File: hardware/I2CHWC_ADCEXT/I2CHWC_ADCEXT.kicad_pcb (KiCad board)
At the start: 2 copper layers, 66 x 99.1 mm, 23 parts, among them J1 ADC 1-8, J10 EXT, J2 ADC 9-16, J3 ADC 17-24, J4 ADC 25-32, J5 ADC 33-40, J6 ADC 41-48, J7 ADC 49-56, J8 ADC 57-64, J9 ADC, U1 4051, U2 4051, U3 4051, U4 4051, U5 4051, U6 4051, U7 4051, U8 4051

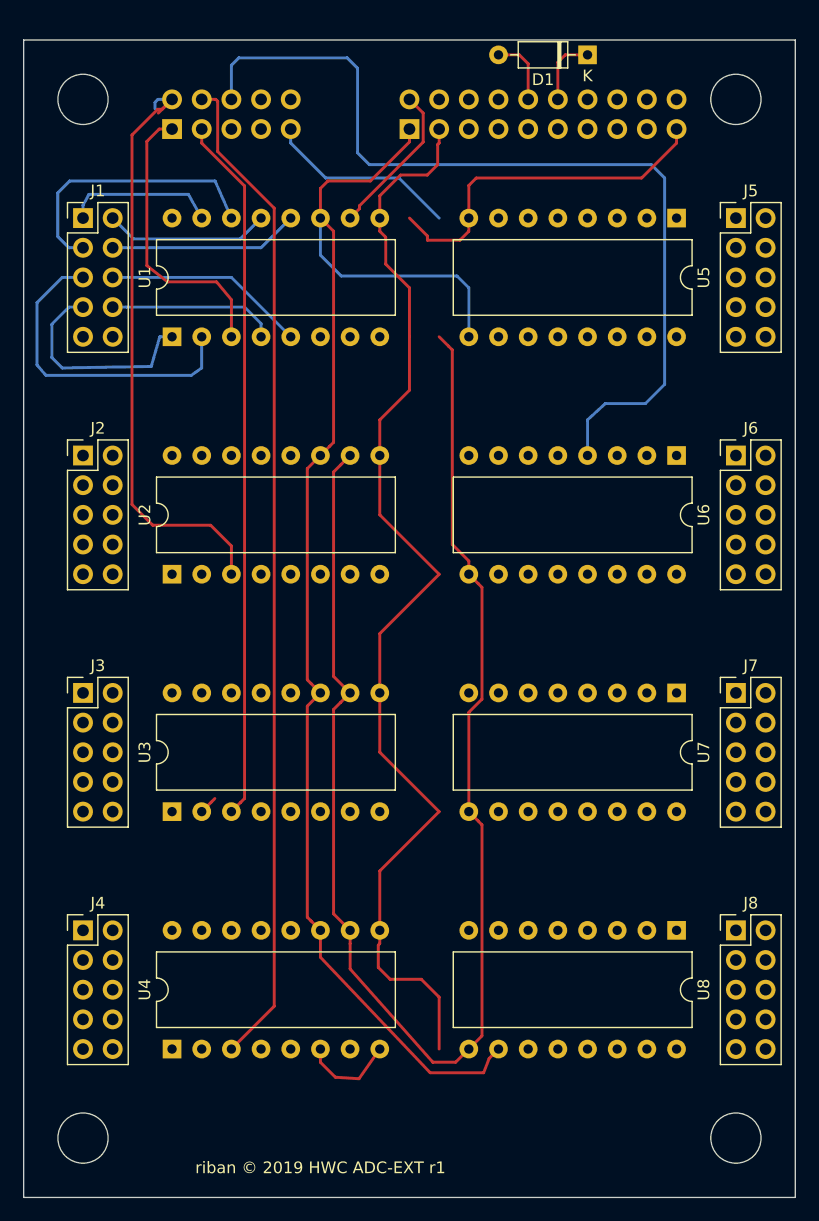
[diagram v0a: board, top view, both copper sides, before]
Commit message: Firmwware changes: Temporarily disable ADC (whilst investigating noise issues). Change quantity of switches (from 60 to 50). Start implementing I2C commands (wip). Reverse encoder rotation (maybe just the hardware implementation of the prototype - need to validate with schematics). Schematic and PCB improvements (wip): Separate out main and extender boards to separate projects / folders. Main board now supports 10 encoders with switches, 20 switches and 8 ADC plus detection of ADC multiplex and I2C address. Extension board for encoders 11 - 30. Extension board for ADC 1 - 64.
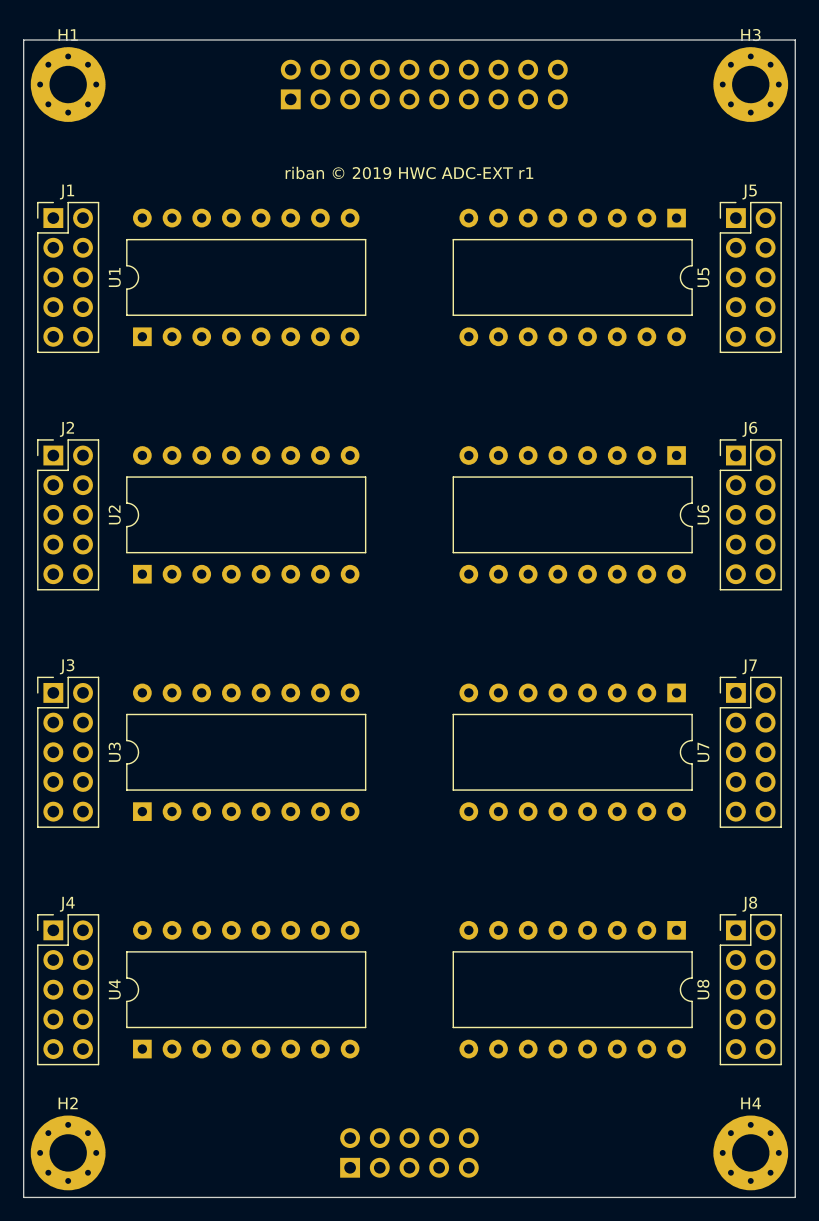
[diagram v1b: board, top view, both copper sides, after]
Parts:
- removed D1: 1N4148, Diode_THT:D_DO-35_SOD27_P7.62mm_Horizontal
- removed REF** (x4): MountingHole_4.3mm_M4, MountingHole:MountingHole_4.3mm_M4
- added H1: MountingHole_Pad, MountingHole:MountingHole_3.2mm_M3_Pad_Via, F.Cu at (39.4, 31.8)
- added H2: MountingHole_Pad, MountingHole:MountingHole_3.2mm_M3_Pad_Via, F.Cu at (39.4, 123.2)
- added H3: MountingHole_Pad, MountingHole:MountingHole_3.2mm_M3_Pad_Via, F.Cu at (97.8, 31.8)
- added H4: MountingHole_Pad, MountingHole:MountingHole_3.2mm_M3_Pad_Via, F.Cu at (97.8, 123.2)
- moved J9 90.2 mm to (63.5, 124.5)
- moved J10 10.5 mm to (58.4, 33.0)
- moved J1 2.54 mm to (38.1, 43.2)
- moved J2 2.54 mm to (38.1, 63.5)
- moved J3 2.54 mm to (38.1, 83.8)
- moved J4 2.54 mm to (38.1, 104.1)
- moved U1 2.54 mm to (45.7, 53.3)
- moved U2 2.54 mm to (45.7, 73.7)
- moved U3 2.54 mm to (45.7, 94.0)
- moved U4 2.54 mm to (45.7, 114.3)
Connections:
- J10 pad 10: Net-(D1-Pad2) -> Net-(J10-Pad10)
- J10 pad 12: Net-(D1-Pad1) -> (no net)
- J10 pad 18: (no net) -> Net-(J10-Pad10)
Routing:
- net MatrixOut2: track 137.6 -> 0.00 mm
- net MatrixOut1: track 120.9 -> 0.00 mm
- net MatrixOut3: track 96.5 -> 0.00 mm
- net ADC4: track 86.1 -> 0.00 mm
- net ADC6: track 77.3 -> 0.00 mm
- net ADC3: track 60.4 -> 0.00 mm
- net ADC2: track 52.5 -> 0.00 mm
- net GND: track 38.9 -> 0.00 mm
- net Net-(J1-Pad5): track 27.5 -> 0.00 mm
- net ADC1: track 24.8 -> 0.00 mm
- net Net-(J1-Pad3): track 23.6 -> 0.00 mm
- net Net-(J1-Pad7): track 18.7 -> 0.00 mm
- net Net-(J1-Pad6): track 17.3 -> 0.00 mm
- net GNDA: track 16.6 -> 0.00 mm
- net Net-(J1-Pad4): track 16.3 -> 0.00 mm
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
